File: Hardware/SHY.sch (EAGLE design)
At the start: 14 parts

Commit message: add few components
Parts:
- added U$1: LSM6DS3_CAST, LinnesLab-Sensors:LSM6DS3_CAST
- added U1: (no value), LinnesLab-Microcontrollers:ARTEMIS.CAST
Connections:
- new net SCL: U$1.SCL
- new net SDA: U$1.SDA
- net GND: now also U$1.GND
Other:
- moved on the sheet: C1, C2, C3, C4, CHRG1, D1, D2, J1, LDO1, R1, R2, R3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

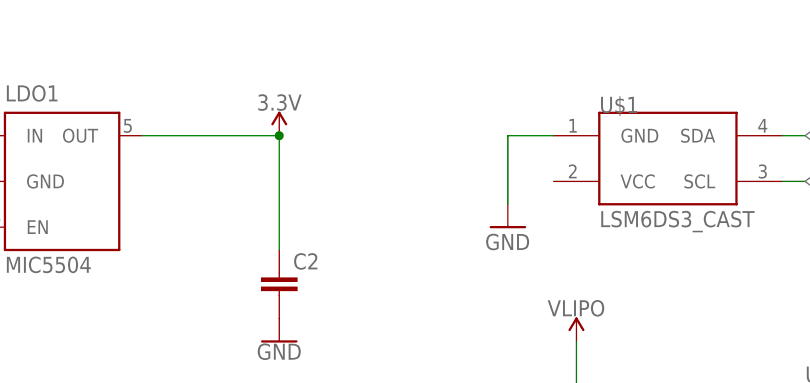
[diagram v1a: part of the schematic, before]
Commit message: Add 3.3v and gnd
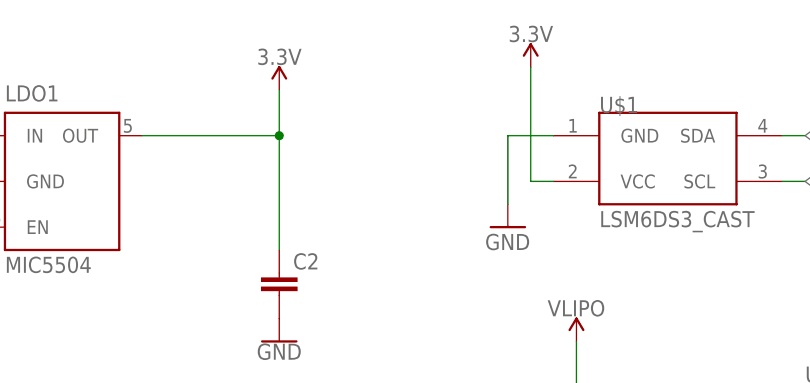
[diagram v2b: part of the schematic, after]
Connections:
- net 3.3V: now also U$1.VCC
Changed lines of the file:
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@@
 <part name="GND10" library="LinnesLab-Symbols" deviceset="GND" device=""/>
 <part name="GND11" library="supply1" library_urn="urn:adsk.eagle:library:371" deviceset="GND" device=""/>
+<part name="SUPPLY7" library="LinnesLab-Symbols" deviceset="3.3V" device=""/>
 </parts>
 <sheets>
@@
 <attribute name="VALUE" x="-187.96" y="91.186" size="1.778" layer="96" align="top-center"/>
 </instance>
-<instance part="SUPPLY1" gate="G$1" x="-106.68" y="99.06" smashed="yes">
-<attribute name="VALUE" x="-106.68" y="101.854" size="1.778" layer="96" align="bottom-center"/>
+<instance part="SUPPLY1" gate="G$1" x="-106.68" y="104.14" smashed="yes">
+<attribute name="VALUE" x="-106.68" y="106.934" size="1.778" layer="96" align="bottom-center"/>
 </instance>
 <instance part="SUPPLY2" gate="VDD" x="-165.1" y="104.14" smashed="yes">
@@
 <instance part="GND11" gate="1" x="-81.28" y="88.9" smashed="yes">
 <attribute name="VALUE" x="-83.82" y="86.36" size="1.778" layer="96"/>
+</instance>
+<instance part="SUPPLY7" gate="G$1" x="-78.74" y="106.68" smashed="yes">
+<attribute name="VALUE" x="-78.74" y="109.474" size="1.778" layer="96" align="bottom-center"/>
 </instance>
 </instances>
@@
 <wire x1="-109.22" y1="50.8" x2="-109.22" y2="53.34" width="0.1524" layer="91"/>
 <wire x1="-109.22" y1="53.34" x2="-119.38" y2="53.34" width="0.1524" layer="91"/>
-</segment>
-</net>
-<net name="3.3V" class="0">
-<segment>
-<pinref part="LDO1" gate="G$1" pin="OUT"/>
-<pinref part="C2" gate="G$1" pin="1"/>
-<wire x1="-121.92" y1="99.06" x2="-106.68" y2="99.06" width="0.1524" layer="91"/>
-<wire x1="-106.68" y1="99.06" x2="-106.68" y2="86.36" width="0.1524" layer="91"/>
-<pinref part="SUPPLY1" gate="G$1" pin="3.3V"/>
-<junction x="-106.68" y="99.06"/>
 </segment>
 </net>
@@
 </segment>
 </net>
+<net name="3.3V" class="0">
+<segment>
+<pinref part="LDO1" gate="G$1" pin="OUT"/>
+<pinref part="C2" gate="G$1" pin="1"/>
+<wire x1="-121.92" y1="99.06" x2="-106.68" y2="99.06" width="0.1524" layer="91"/>
+<wire x1="-106.68" y1="99.06" x2="-106.68" y2="86.36" width="0.1524" layer="91"/>
+<pinref part="SUPPLY1" gate="G$1" pin="3.3V"/>
+<wire x1="-106.68" y1="104.14" x2="-106.68" y2="99.06" width="0.1524" layer="91"/>
+<junction x="-106.68" y="99.06"/>
+</segment>
+<segment>
+<pinref part="U$1" gate="G$1" pin="VCC"/>
+<pinref part="SUPPLY7" gate="G$1" pin="3.3V"/>
+<wire x1="-76.2" y1="93.98" x2="-78.74" y2="93.98" width="0.1524" layer="91"/>
+<wire x1="-78.74" y1="93.98" x2="-78.74" y2="106.68" width="0.1524" layer="91"/>
+</segment>
+</net>

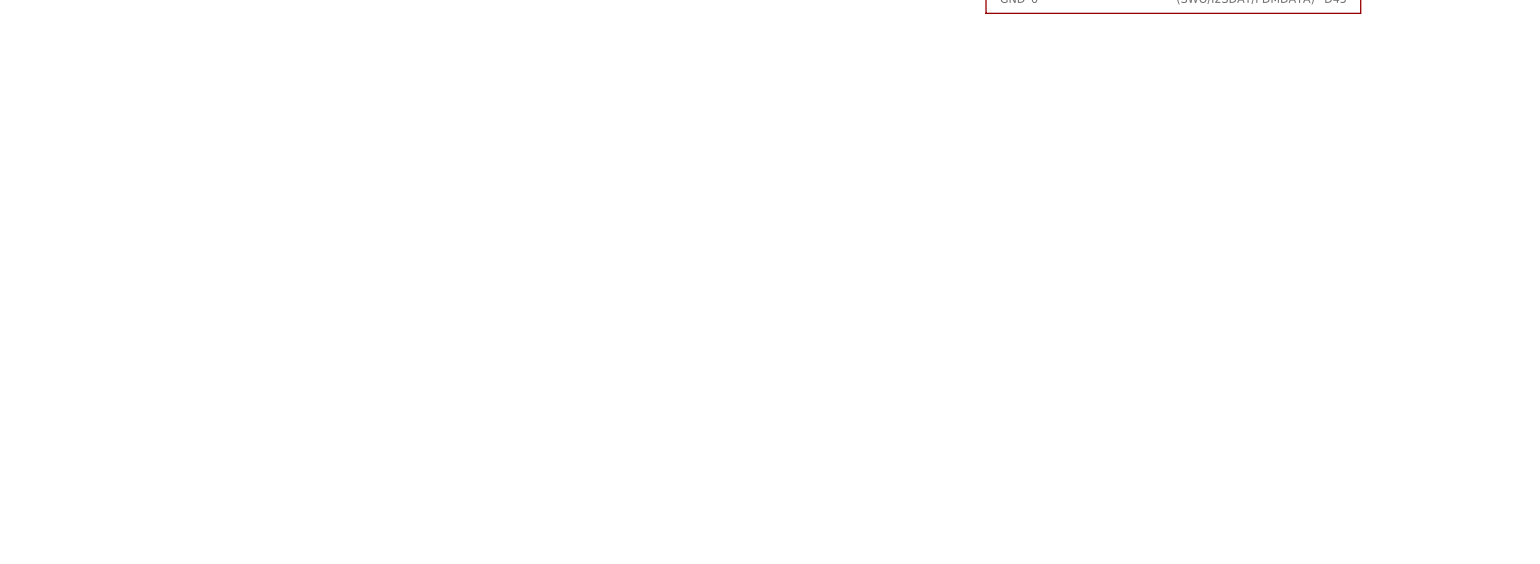
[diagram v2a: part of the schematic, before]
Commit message: Add some resistors and compacitors
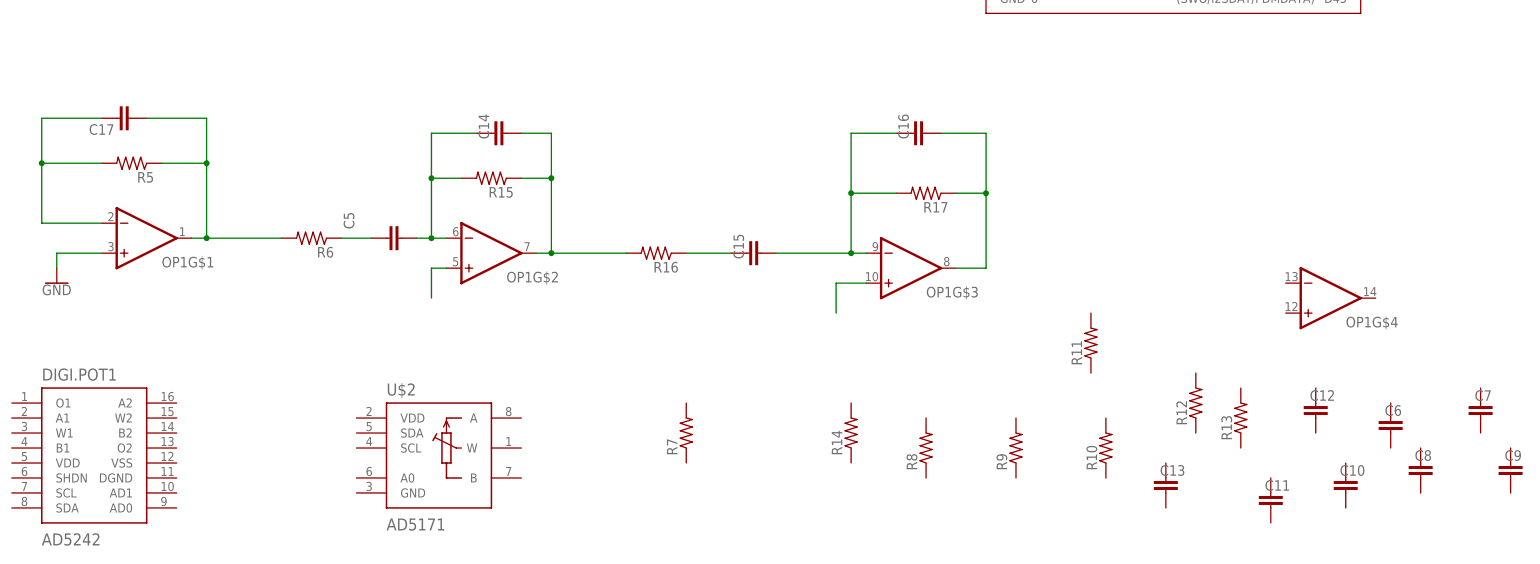
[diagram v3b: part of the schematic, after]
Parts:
- added C10, C11, C12, C13, C14, C15, C16, C17, C5, C6, C7, C8, C9: (no value), LinnesLab-Passives:CAPACITOR0603
- added DIGI.POT1: AD5242, LinnesLab-DigitalIC:AD5242
- added OP1: (no value), LinnesLab-AnalogIC:OP-QUAD-SO14
- added R10, R11, R12, R13, R14, R15, R16, R17, R5, R6, R7, R8, R9: (no value), LinnesLab-Passives:RESISTOR0603
- added U$2: AD5171, LinnesLab-DigitalIC:AD5171
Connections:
- new net N$10: C15.2, C16.1, OP1G$3.-IN, R17.2
- new net N$11: C16.2, OP1G$3.OUT, R17.1
- new net N$12: OP1G$2.+IN
- new net N$13: OP1G$3.+IN
- new net N$2: C17.1, OP1G$1.-IN, R5.2
- new net N$3: C17.2, OP1G$1.OUT, R5.1, R6.2
- new net N$4: C15.1, R16.1
- new net N$7: C14.2, OP1G$2.OUT, R15.1, R16.2
- new net N$8: C5.1, R6.1
- new net N$9: C14.1, C5.2, OP1G$2.-IN, R15.2
- net GND: now also OP1G$1.+IN
